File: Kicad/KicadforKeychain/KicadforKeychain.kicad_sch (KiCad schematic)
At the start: 8 parts

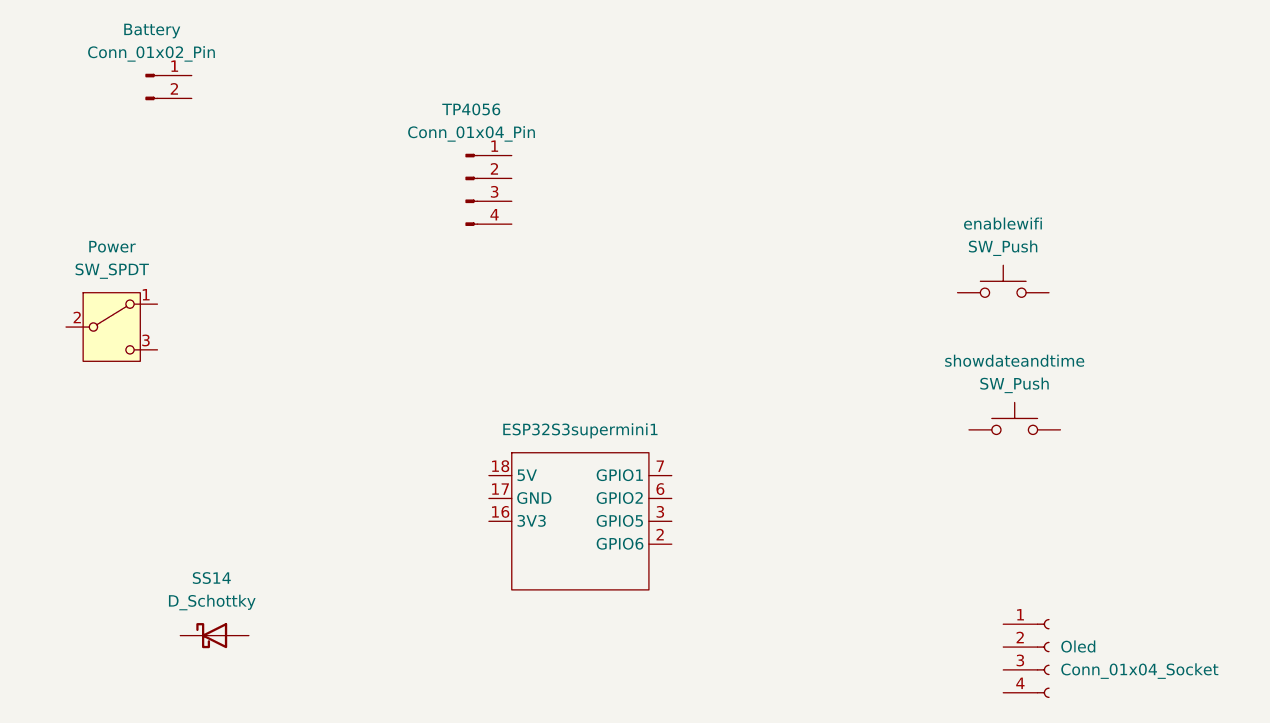
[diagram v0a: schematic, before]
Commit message: sch complete made costom footprints and added to pcb i have kept everthing in pcb in place now moving with wiring
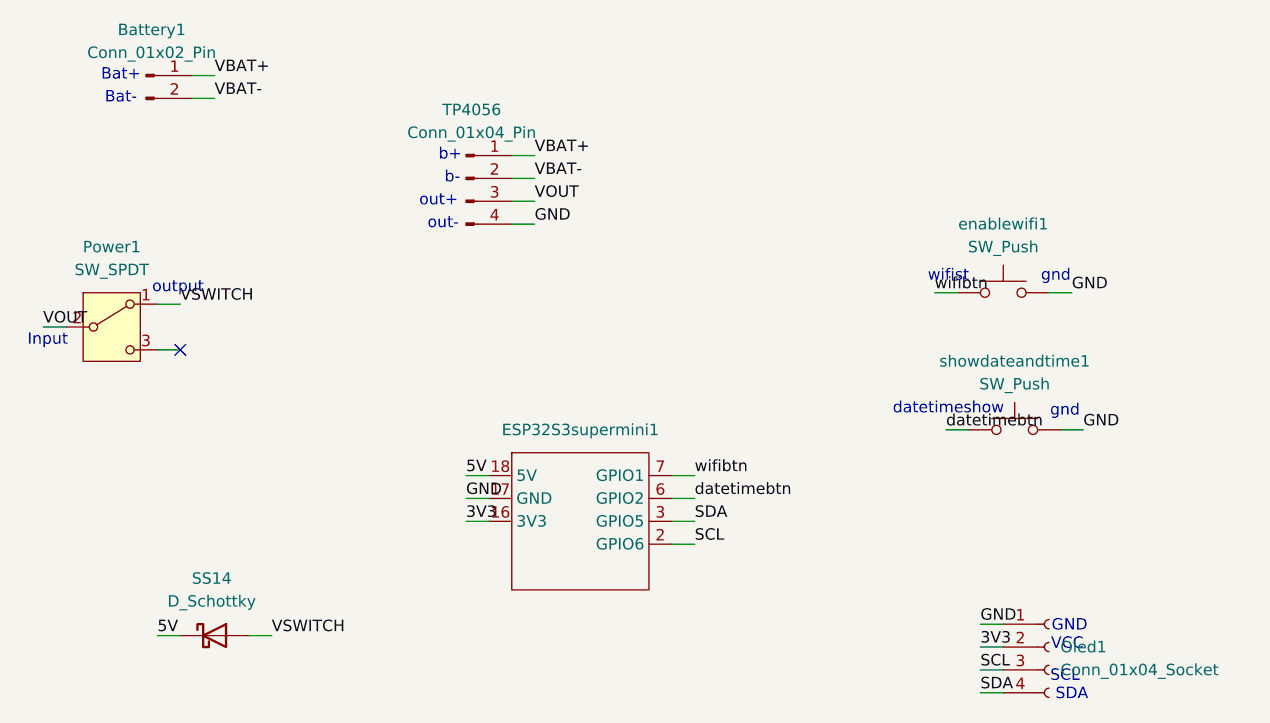
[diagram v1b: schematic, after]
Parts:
- Battery1: renamed from Battery; footprint (none) -> Keychain:Battery
- ESP32S3supermini1: footprint RF_Module:ESP32-C3-WROOM-02 -> Keychain:ESP32S3mini
- Oled1: renamed from Oled; footprint Display:ER_OLEDM0.91_1x-I2C -> Connector_PinHeader_2.54mm:PinHeader_1x04_P2.54mm_Vertical
- Power1: renamed from Power; footprint Package_SON:WSON-8-1EP_6x5mm_P1.27mm_EP3.4x4mm -> Keychain:slideswitch
- SS14: footprint (none) -> Diode_SMD:D_SMA
- TP4056: footprint (none) -> Keychain:tp4056
- enablewifi1: renamed from enablewifi; footprint Button_Switch_SMD:Nidec_Copal_CAS-120A -> Button_Switch_THT:SW_PUSH_6mm
- showdateandtime1: renamed from showdateandtime; footprint (none) -> Button_Switch_THT:SW_PUSH_6mm
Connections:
- net 5V: now reaches SS14.1 (K)
- net 5V: now also ESP32S3supermini1.18 (5V)
- net VSWITCH: now reaches SS14.2 (A)
- net VSWITCH: now also Power1.1 (A)
- net VBAT+: now reaches TP4056.1 (Pin_1)
- net VBAT+: now also Battery1.1 (Pin_1)
- net VBAT-: now reaches TP4056.2 (Pin_2)
- net VBAT-: now also Battery1.2 (Pin_2)
- net VOUT: now reaches TP4056.3 (Pin_3)
- net VOUT: now also Power1.2 (B)
- net GND: now reaches TP4056.4 (Pin_4)
- net GND: now also ESP32S3supermini1.17 (GND), Oled1.1 (Pin_1), enablewifi1.2, showdateandtime1.2
- net datetimebtn: now reaches showdateandtime1.1
- net datetimebtn: now also ESP32S3supermini1.6 (GPIO2)
- net wifibtn: now reaches enablewifi1.1
- net wifibtn: now also ESP32S3supermini1.7 (GPIO1)
- net 3V3: now reaches ESP32S3supermini1.16 (3V3)
- net 3V3: now also Oled1.2 (Pin_2)
- net SCL: now reaches ESP32S3supermini1.2 (GPIO6)
- net SCL: now also Oled1.3 (Pin_3)
- net SDA: now reaches ESP32S3supermini1.3 (GPIO5)
- net SDA: now also Oled1.4 (Pin_4)
- no-connect marks 0 -> 1
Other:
- note added: "Bat+"
- note added: "Bat-"
- note added: "GND"
- note added: "Input"
- note added: "SCL"
- note added: "SDA"
- note added: "VCC"
- note added: "b+"
- note added: "b-"
- note added: "datetimeshow"
- note added: "gnd"
- note added: "out+"
- note added: "out-"
- note added: "output"
- note added: "wifist"
